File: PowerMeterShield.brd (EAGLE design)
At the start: 71.1 x 53.3 mm, 34 parts, among them U1 INA170EA/2K5, U2 THS4521, U3 INA138, U4 ADUM1250ARZ, U5 MCP3426A0-E/SN, U6 ISL21080

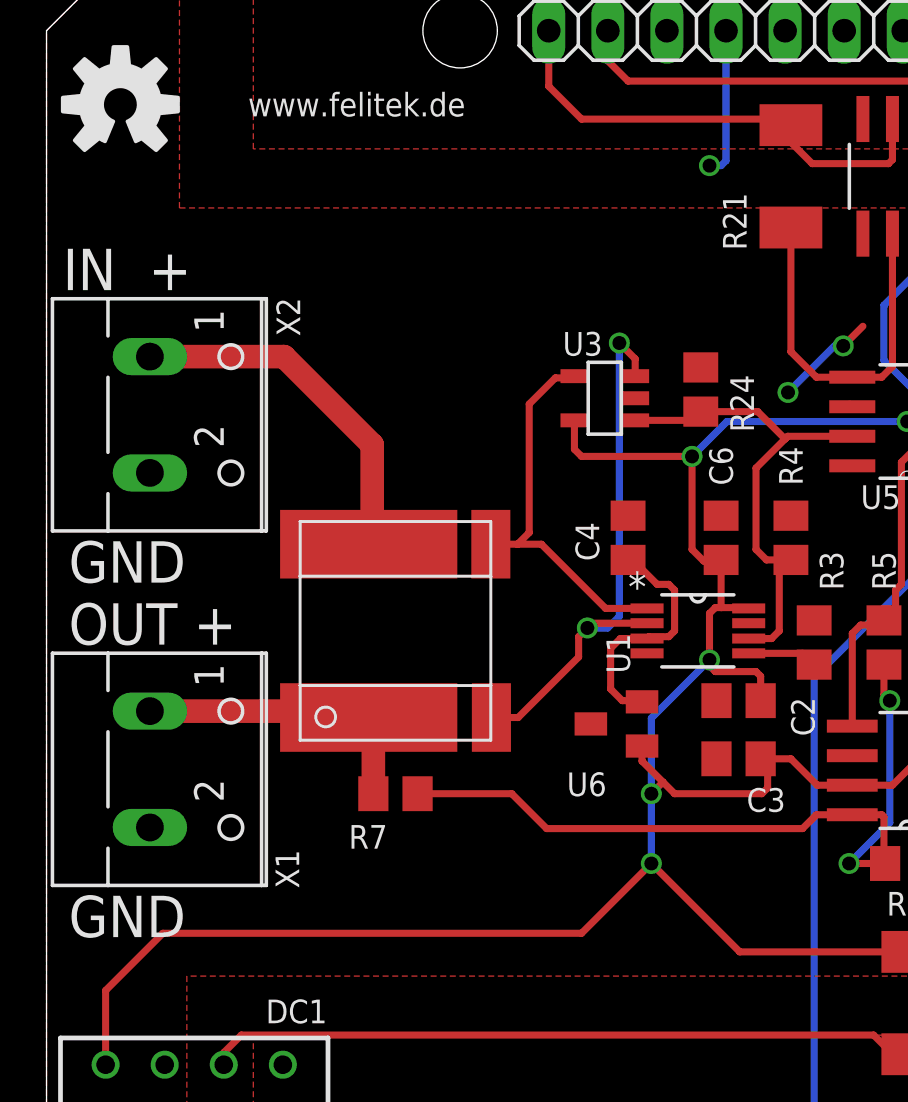
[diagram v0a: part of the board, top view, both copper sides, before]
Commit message: Fixed trace width, added polyfuse
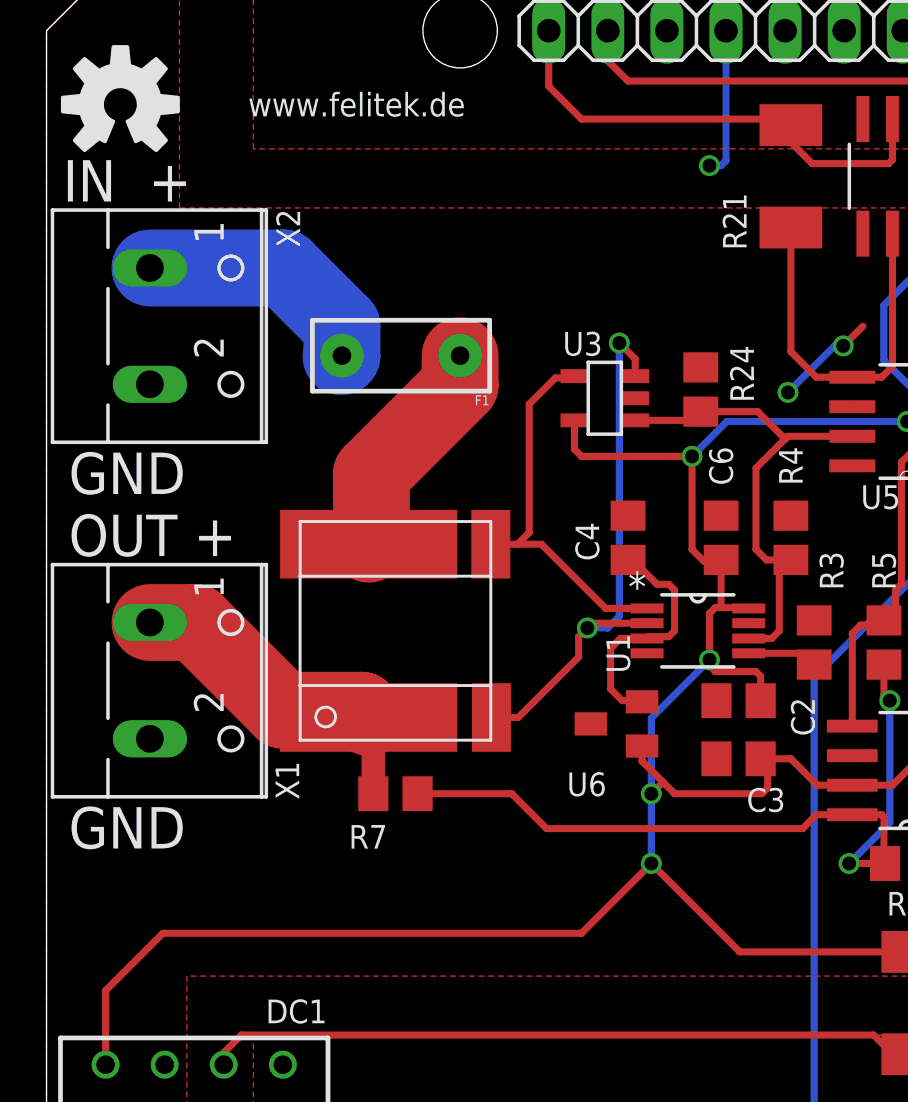
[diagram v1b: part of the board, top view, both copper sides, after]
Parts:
- added F1: PTCPTH, SparkFun:PTC
- moved X2 3.81 mm to (5.71, 38.1)
- moved X1 3.81 mm to (5.71, 22.9)
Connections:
- new net N$3: F1.P$1, R1.I1
- net VIN_MEAS: now also F1.P$2; no longer R1.I1
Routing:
- net N$3: track 0.00 -> 9.73 mm
- net VIN_MEAS: track 15.5 -> 10.6 mm
- net V_MEAS: track 12.9 -> 14.5 mm
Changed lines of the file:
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@@
 <setting verticaltext="up"/>
 </settings>
-<grid distance="0.05" unitdist="inch" unit="inch" style="lines" multiple="1" display="no" altdistance="0.025" altunitdist="inch" altunit="inch"/>
+<grid distance="50" unitdist="mil" unit="mil" style="lines" multiple="1" display="no" altdistance="0.025" altunitdist="inch" altunit="inch"/>
 <layers>
 <layer number="1" name="Top" color="4" fill="1" visible="yes" active="yes"/>
@@
 <hole x="17.78" y="50.8" drill="3.2"/>
 <hole x="68.58" y="7.62" drill="3.2"/>
-<text x="0.7025" y="39.6475" size="1.778" layer="25">IN  +</text>
-<text x="0.9525" y="24.4075" size="1.778" layer="25">OUT +</text>
-<text x="0.9525" y="28.8525" size="1.778" layer="25" align="top-left">GND</text>
-<text x="0.9525" y="13.6125" size="1.778" layer="25" align="top-left">GND</text>
+<text x="0.7025" y="43.4575" size="1.778" layer="25">IN  +</text>
+<text x="0.9525" y="28.2175" size="1.778" layer="25">OUT +</text>
+<text x="0.9525" y="32.6625" size="1.778" layer="25" align="top-left">GND</text>
+<text x="0.9525" y="17.4225" size="1.778" layer="25" align="top-left">GND</text>
 <text x="55.54" y="26.27" size="1.27" layer="21" rot="R90" align="bottom-center">I²C Current and Voltage Meter Shield
 </text>
@@
 <attribute name="OC_FARNELL" value="1107419RL" x="60.72" y="-35.96" size="1.778" layer="27" display="off"/>
 </element>
-<element name="X1" library="con-wago-500" package="W237-102" value="" x="5.715" y="19.05" smashed="yes" rot="R270">
-<attribute name="PRICE_10" value="0.294" x="-55.245" y="-36.83" size="1.778" layer="27" rot="R270" display="off"/>
-<attribute name="OC_NEWARK" value="70K9898" x="-55.245" y="-36.83" size="1.778" layer="27" rot="R270" display="off"/>
-<attribute name="MPN" value="237-102" x="-55.245" y="-36.83" size="1.778" layer="27" rot="R270" display="off"/>
-<attribute name="MF" value="" x="-55.245" y="-36.83" size="1.778" layer="27" rot="R270" display="off"/>
-<attribute name="OC_FARNELL" value="1717001" x="-55.245" y="-36.83" size="1.778" layer="27" rot="R270" display="off"/>
-<attribute name="VALUE" x="-1.905" y="24.09" size="1.27" layer="27" ratio="10" rot="R270"/>
-<attribute name="NAME" x="10.3538" y="13.9338" size="1.016" layer="25" ratio="10" rot="R90" align="center-left"/>
-</element>
-<element name="X2" library="con-wago-500" package="W237-102" value="" x="5.715" y="34.29" smashed="yes" rot="R270">
-<attribute name="PRICE_10" value="0.294" x="-55.245" y="-31.75" size="1.778" layer="27" rot="R270" display="off"/>
-<attribute name="OC_NEWARK" value="70K9898" x="-55.245" y="-31.75" size="1.778" layer="27" rot="R270" display="off"/>
-<attribute name="MPN" value="237-102" x="-55.245" y="-31.75" size="1.778" layer="27" rot="R270" display="off"/>
-<attribute name="MF" value="" x="-55.245" y="-31.75" size="1.778" layer="27" rot="R270" display="off"/>
-<attribute name="OC_FARNELL" value="1717001" x="-55.245" y="-31.75" size="1.778" layer="27" rot="R270" display="off"/>
-<attribute name="VALUE" x="-1.905" y="39.33" size="1.27" layer="27" ratio="10" rot="R270"/>
-<attribute name="NAME" x="10.3962" y="39.3262" size="1.016" layer="25" ratio="10" rot="R270" align="center-left"/>
+<element name="X1" library="con-wago-500" package="W237-102" value="" x="5.715" y="22.86" smashed="yes" rot="R270">
+<attribute name="PRICE_10" value="0.294" x="-55.245" y="-33.02" size="1.778" layer="27" rot="R270" display="off"/>
+<attribute name="OC_NEWARK" value="70K9898" x="-55.245" y="-33.02" size="1.778" layer="27" rot="R270" display="off"/>
+<attribute name="MPN" value="237-102" x="-55.245" y="-33.02" size="1.778" layer="27" rot="R270" display="off"/>
+<attribute name="MF" value="" x="-55.245" y="-33.02" size="1.778" layer="27" rot="R270" display="off"/>
+<attribute name="OC_FARNELL" value="1717001" x="-55.245" y="-33.02" size="1.778" layer="27" rot="R270" display="off"/>
+<attribute name="VALUE" x="-1.905" y="27.9" size="1.27" layer="27" ratio="10" rot="R270"/>
+<attribute name="NAME" x="10.3538" y="17.7438" size="1.016" layer="25" ratio="10" rot="R90" align="center-left"/>
+</element>
+<element name="X2" library="con-wago-500" package="W237-102" value="" x="5.715" y="38.1" smashed="yes" rot="R270">
+<attribute name="PRICE_10" value="0.294" x="-55.245" y="-27.94" size="1.778" layer="27" rot="R270" display="off"/>
+<attribute name="OC_NEWARK" value="70K9898" x="-55.245" y="-27.94" size="1.778" layer="27" rot="R270" display="off"/>
+<attribute name="MPN" value="237-102" x="-55.245" y="-27.94" size="1.778" layer="27" rot="R270" display="off"/>
+<attribute name="MF" value="" x="-55.245" y="-27.94" size="1.778" layer="27" rot="R270" display="off"/>
+<attribute name="OC_FARNELL" value="1717001" x="-55.245" y="-27.94" size="1.778" layer="27" rot="R270" display="off"/>
+<attribute name="VALUE" x="-1.905" y="43.14" size="1.27" layer="27" ratio="10" rot="R270"/>
+<attribute name="NAME" x="10.3962" y="43.1362" size="1.016" layer="25" ratio="10" rot="R270" align="center-left"/>
 </element>
 <element name="U5" library="MCP3428" package="SOIC127P600X175-8N" value="MCP3426A0-E/SN" x="37" y="34" smashed="yes" rot="R180">
@@
 </element>
 <element name="R24" library="rcl" package="R0805" value="20k" x="28.125" y="35.375" smashed="yes" rot="R270">
-<attribute name="NAME" x="29.395" y="36.01" size="1.016" layer="25" rot="R270"/>
+<attribute name="NAME" x="29.395" y="37.28" size="1.016" layer="25" rot="R270"/>
 </element>
 <element name="R22" library="rcl" package="R2010" value="0" x="37.24" y="9" smashed="yes" rot="R270">
@@
 <element name="R23" library="rcl" package="R2010" value="0" x="42.73" y="9" smashed="yes" rot="R270">
 <attribute name="NAME" x="44.635" y="12.175" size="1.016" layer="25" rot="R270"/>
+</element>
+<element name="F1" library="SparkFun" package="PTC" value="PTCPTH" x="15.24" y="36.83" rot="R180">
+<attribute name="PRICE_10" value="0.59" x="15.24" y="36.83" size="1.778" layer="27" rot="R180" display="off"/>
+<attribute name="OC_DIGIKEY" value="RGEF1000-ND" x="15.24" y="36.83" size="1.778" layer="27" rot="R180" display="off"/>
 </element>
 </elements>
@@
 <signal name="VIN_MEAS" class="1">
 <contactref element="X2" pad="1"/>
-<contactref element="R1" pad="I1"/>
-<wire x1="4.445" y1="36.79" x2="10.21" y2="36.79" width="1.016" layer="1"/>
-<wire x1="10.21" y1="36.79" x2="14" y2="33" width="1.016" layer="1"/>
-<wire x1="14" y1="33" x2="14" y2="28.875" width="1.016" layer="1"/>
-<wire x1="14" y1="28.875" x2="13.85" y2="28.725" width="1.016" layer="1"/>
+<contactref element="F1" pad="P$2"/>
+<wire x1="12.66" y1="36.79" x2="12.7" y2="36.83" width="3.302" layer="16"/>
+<wire x1="4.445" y1="40.6" x2="10.2" y2="40.6" width="3.302" layer="16"/>
+<wire x1="10.2" y1="40.6" x2="12.7" y2="38.1" width="3.302" layer="16"/>
+<wire x1="12.7" y1="38.1" x2="12.7" y2="36.83" width="3.302" layer="16"/>
 </signal>
 <signal name="V_MEAS" class="1">
@@
 <contactref element="R1" pad="I2"/>
 <contactref element="R7" pad="1"/>
-<wire x1="4.445" y1="21.55" x2="13.575" y2="21.55" width="1.016" layer="1"/>
-<wire x1="13.575" y1="21.55" x2="13.85" y2="21.275" width="1.016" layer="1"/>
 <wire x1="14.05" y1="18" x2="14.05" y2="21.075" width="1.016" layer="1"/>
 <wire x1="14.05" y1="21.075" x2="13.85" y2="21.275" width="1.016" layer="1"/>
+<wire x1="4.445" y1="25.36" x2="6.39" y2="25.36" width="3.302" layer="1"/>
+<wire x1="6.39" y1="25.36" x2="10.16" y2="21.59" width="3.302" layer="1"/>
+<wire x1="10.16" y1="21.59" x2="13.535" y2="21.59" width="3.302" layer="1"/>
+<wire x1="13.535" y1="21.59" x2="13.85" y2="21.275" width="3.302" layer="1"/>
 </signal>
 <signal name="ADC2">
@@
 <wire x1="34.5" y1="15" x2="36.05" y2="15" width="0.3048" layer="1"/>
 </signal>
+<signal name="N$3">
+<contactref element="R1" pad="I1"/>
+<contactref element="F1" pad="P$1"/>
+<wire x1="17.78" y1="36.83" x2="17.78" y2="35.56" width="3.302" layer="1"/>
+<wire x1="17.78" y1="35.56" x2="13.97" y2="31.75" width="3.302" layer="1"/>
+<wire x1="13.97" y1="31.75" x2="13.97" y2="28.845" width="3.302" layer="1"/>
+<wire x1="13.97" y1="28.845" x2="13.85" y2="28.725" width="3.302" layer="1"/>
+</signal>
 </signals>

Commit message: Removed obsolete GND via
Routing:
- net GND: track 6.39 -> 0.00 mm, vias 1 -> 0
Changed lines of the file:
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@@
 <contactref element="DC1" pad="1"/>
 <contactref element="U4" pad="4"/>
-<wire x1="29.21" y1="50.8" x2="29.21" y2="45.21" width="0.3048" layer="16"/>
-<via x="28.5" y="45" extent="1-16" drill="0.6"/>
-<wire x1="29.21" y1="45.21" x2="29" y2="45" width="0.3048" layer="16"/>
-<wire x1="29" y1="45" x2="28.5" y2="45" width="0.3048" layer="16"/>
 <contactref element="R23" pad="2"/>
 </signal>

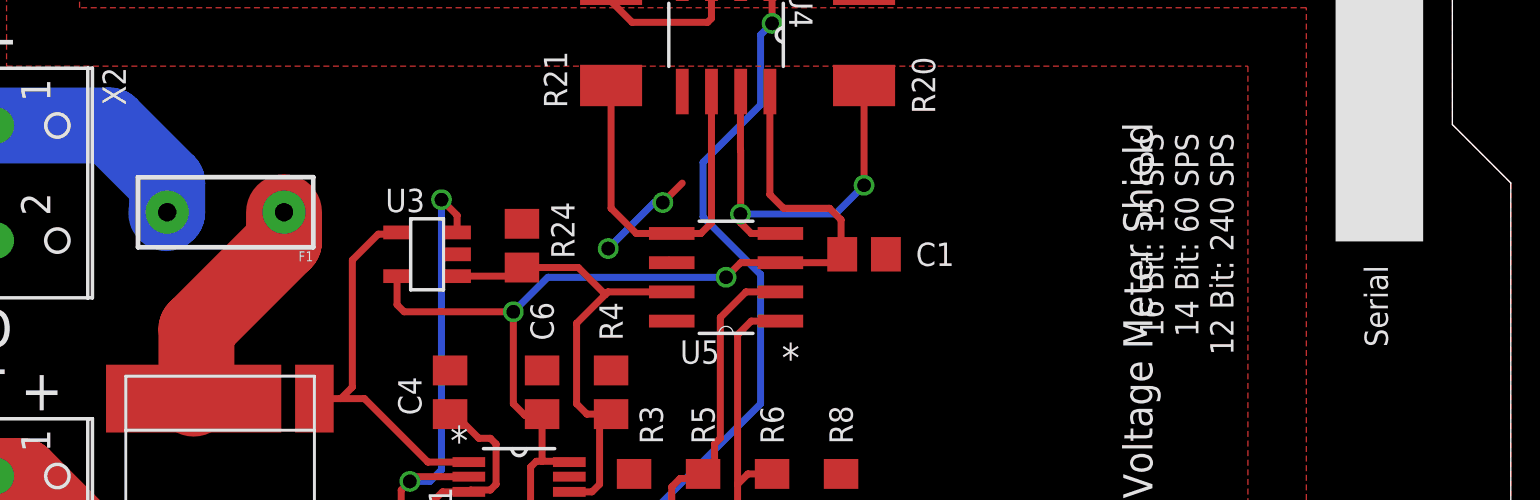
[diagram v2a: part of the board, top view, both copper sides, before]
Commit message: Fixed fuse designator, misc silkscreen fixes
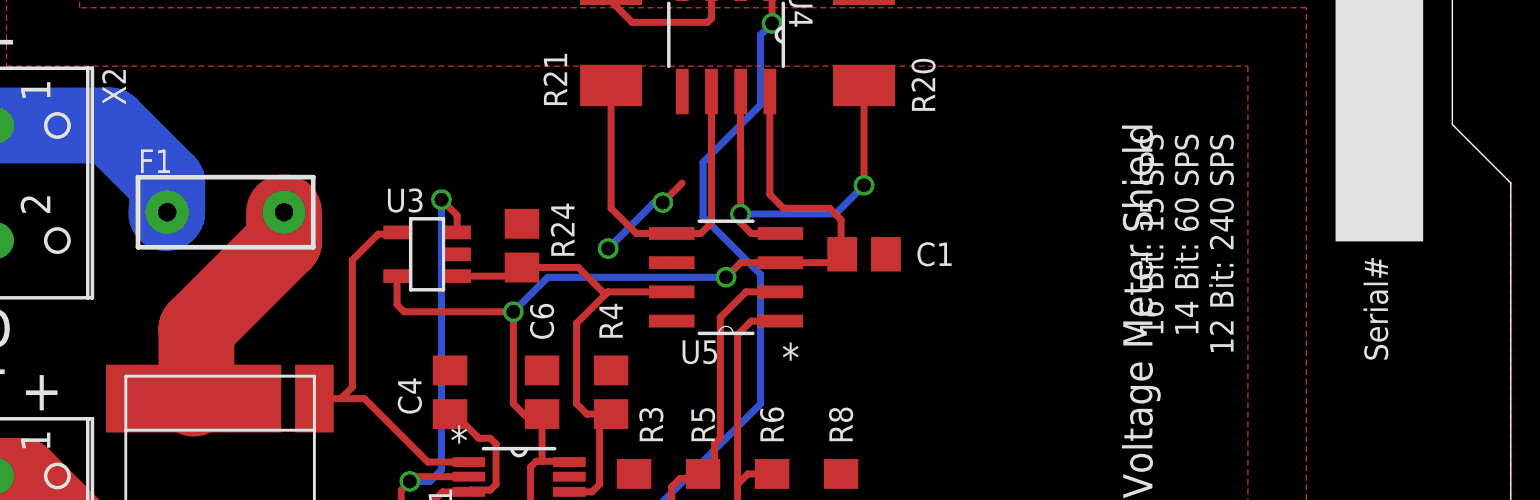
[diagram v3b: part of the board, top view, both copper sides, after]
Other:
- board text added: "Serial#"
- board text removed: "Serial"
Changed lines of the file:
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@@
 <setting verticaltext="up"/>
 </settings>
-<grid distance="50" unitdist="mil" unit="mil" style="lines" multiple="1" display="no" altdistance="0.025" altunitdist="inch" altunit="inch"/>
+<grid distance="0.05" unitdist="inch" unit="inch" style="lines" multiple="1" display="no" altdistance="0.025" altunitdist="inch" altunit="inch"/>
 <layers>
 <layer number="1" name="Top" color="4" fill="1" visible="yes" active="yes"/>
@@
 <text x="13.335" y="47.625" size="1.016" layer="25" align="center">www.felitek.de</text>
 <rectangle x1="63.5" y1="35.56" x2="67.31" y2="48.26" layer="25"/>
-<text x="65.27" y="30.97" size="1.016" layer="25" rot="R90" align="center-left">Serial</text>
+<text x="65.27" y="30.335" size="1.016" layer="25" rot="R90" align="center-left">Serial#</text>
 </plain>
 <attributes>
@@
 <attribute name="NAME" x="44.635" y="12.175" size="1.016" layer="25" rot="R270"/>
 </element>
-<element name="F1" library="SparkFun" package="PTC" value="PTCPTH" x="15.24" y="36.83" rot="R180">
+<element name="F1" library="SparkFun" package="PTC" value="PTCPTH" x="15.24" y="36.83" smashed="yes" rot="R180">
 <attribute name="PRICE_10" value="0.59" x="15.24" y="36.83" size="1.778" layer="27" rot="R180" display="off"/>
 <attribute name="OC_DIGIKEY" value="RGEF1000-ND" x="15.24" y="36.83" size="1.778" layer="27" rot="R180" display="off"/>
+<attribute name="NAME" x="11.43" y="38.535" size="1.016" layer="25"/>
 </element>
 </elements>
